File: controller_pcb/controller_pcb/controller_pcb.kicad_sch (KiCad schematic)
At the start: 31 parts, among them J1 USB_B_Micro, J2 Conn_01x04_Male, SW1 SW_MEC_5E, SW10 SW_MEC_5E, SW11 SW_MEC_5E, SW12 SW_MEC_5E, SW2 SW_MEC_5E, SW3 SW_MEC_5E, SW4 SW_MEC_5E, SW5 SW_MEC_5E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

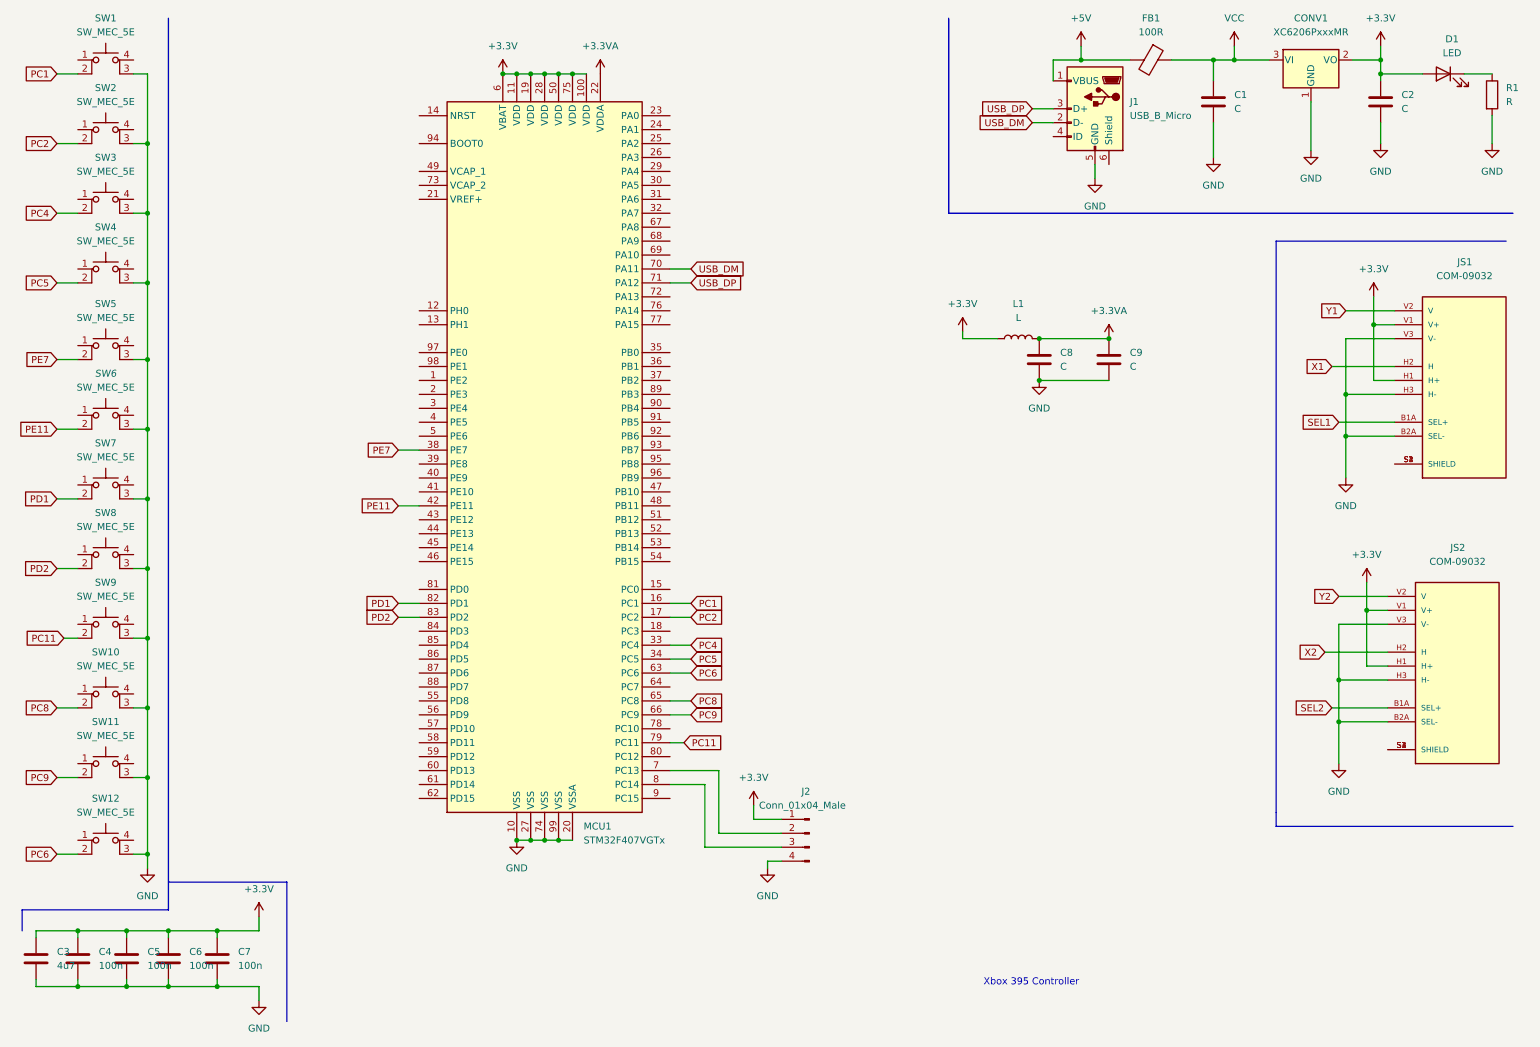
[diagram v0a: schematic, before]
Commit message: have to draw pcb
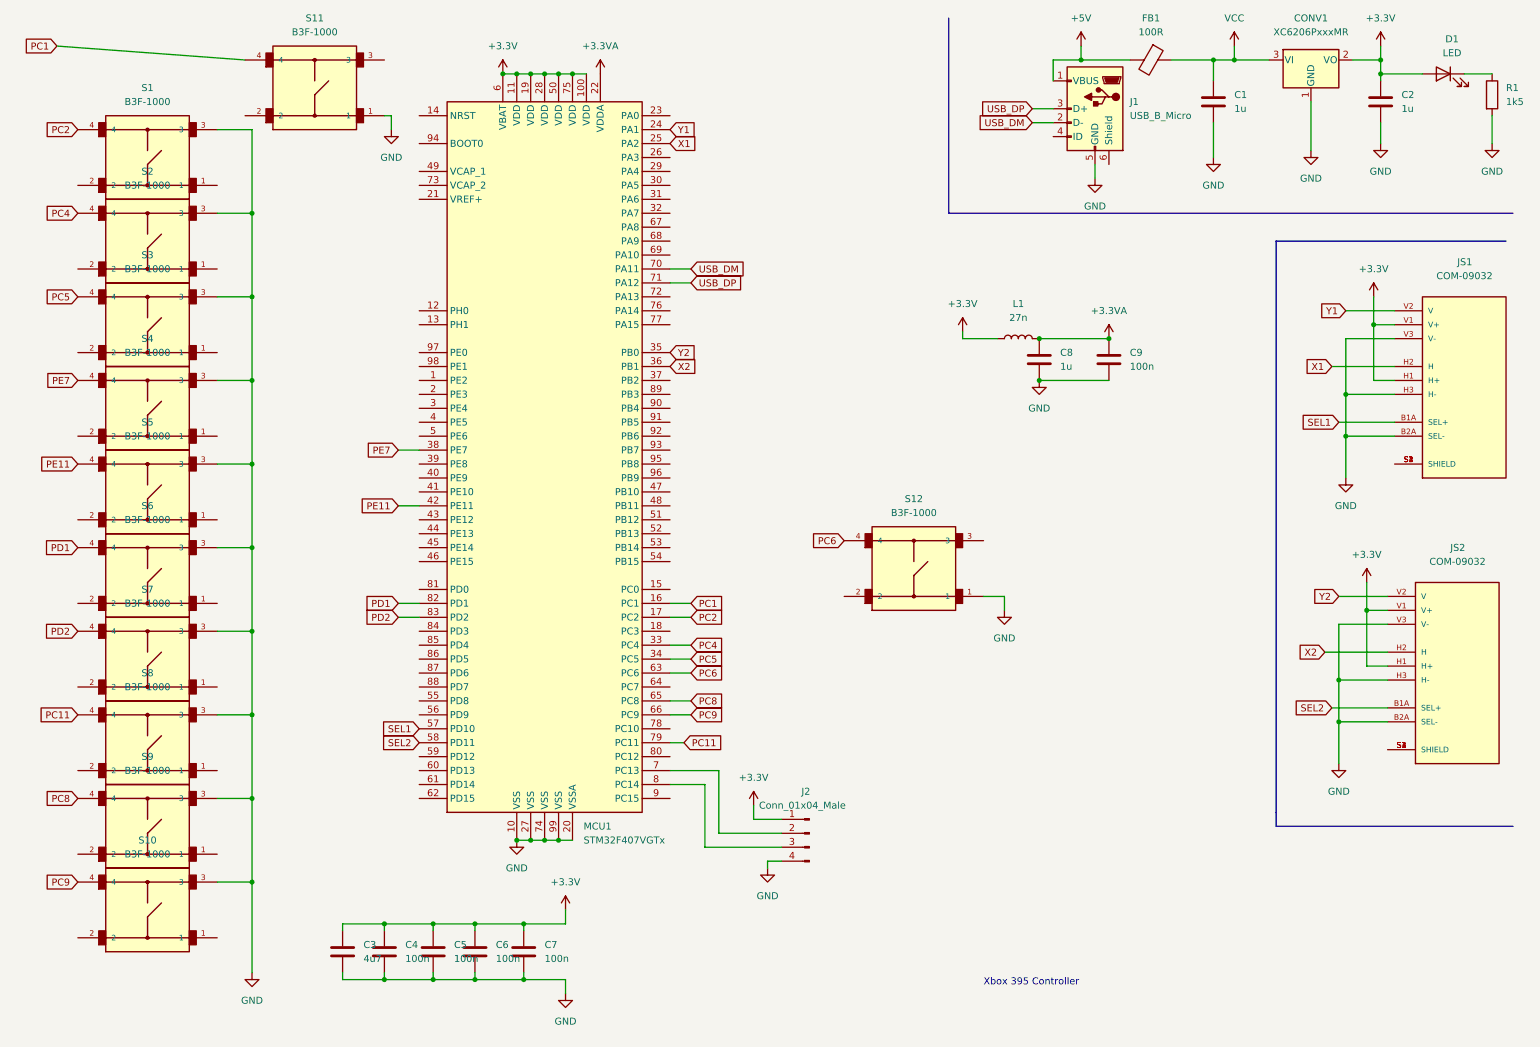
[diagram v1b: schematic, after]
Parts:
- removed SW1, SW10, SW11, SW12, SW2, SW3, SW4, SW5, SW6, SW7, SW8, SW9: SW_MEC_5E, Button_Switch_THT:SW_Tactile_Straight_KSA0Axx1LFTR, symbol Switch:SW_MEC_5E
- added S1, S10, S11, S12, S2, S3, S4, S5, S6, S7, S8, S9: B3F-1000, B3F-1000:SW_B3F-1000, symbol B3F-1000:B3F-1000
- C1, C2, C8: value C -> 1u
- C9: value C -> 100n
- L1: value L -> 27n
- R1: value R -> 1k5
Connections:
- net GND: now also S1.3, S10.3, S11.1, S12.1, S2.3, S3.3, S4.3, S5.3, S6.3, S7.3, S8.3, S9.3
- net PC1: now also S11.4
- net PC11: now also S8.4
- net PC2: now also S1.4
- net PC4: now also S2.4
- net PC5: now also S3.4
- net PC6: now also S12.4
- net PC8: now also S9.4
- net PC9: now also S10.4
- net PD1: now also S6.4
- net PD2: now also S7.4
- net PE11: now also S5.4
- net PE7: now also S4.4
- net SEL1: now also MCU1.57 (PD10)
- net SEL2: now also MCU1.58 (PD11)
- net X1: now also MCU1.25 (PA2)
- net X2: now also MCU1.36 (PB1)
- net Y1: now also MCU1.24 (PA1)
- net Y2: now also MCU1.35 (PB0)
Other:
- moved on the sheet: C3, C4, C5, C6, C7

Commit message: Updated PCB
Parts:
- removed J2: Conn_01x04_Male, Connector_PinHeader_2.54mm:PinHeader_1x04_P2.54mm_Vertical, symbol Connector:Conn_01x04_Male
- added FLASH: JTAG/SWD, symbol Connector_Generic:Conn_02x10_Odd_Even
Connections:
- net +3V3: now also FLASH.1 (Pin_1)
- net GND: now also MCU1.94 (BOOT0), FLASH.10 (Pin_10), FLASH.12 (Pin_12), FLASH.14 (Pin_14), FLASH.16 (Pin_16), FLASH.18 (Pin_18), FLASH.20 (Pin_20), FLASH.4 (Pin_4), FLASH.6 (Pin_6), FLASH.8 (Pin_8)
- net SW_DIO: now reaches MCU1.72 (PA13)
- net SW_DIO: now also FLASH.7 (Pin_7)
- net SW_CLK: now reaches MCU1.76 (PA14)
- net SW_CLK: now also FLASH.9 (Pin_9)
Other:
- moved on the sheet: S12

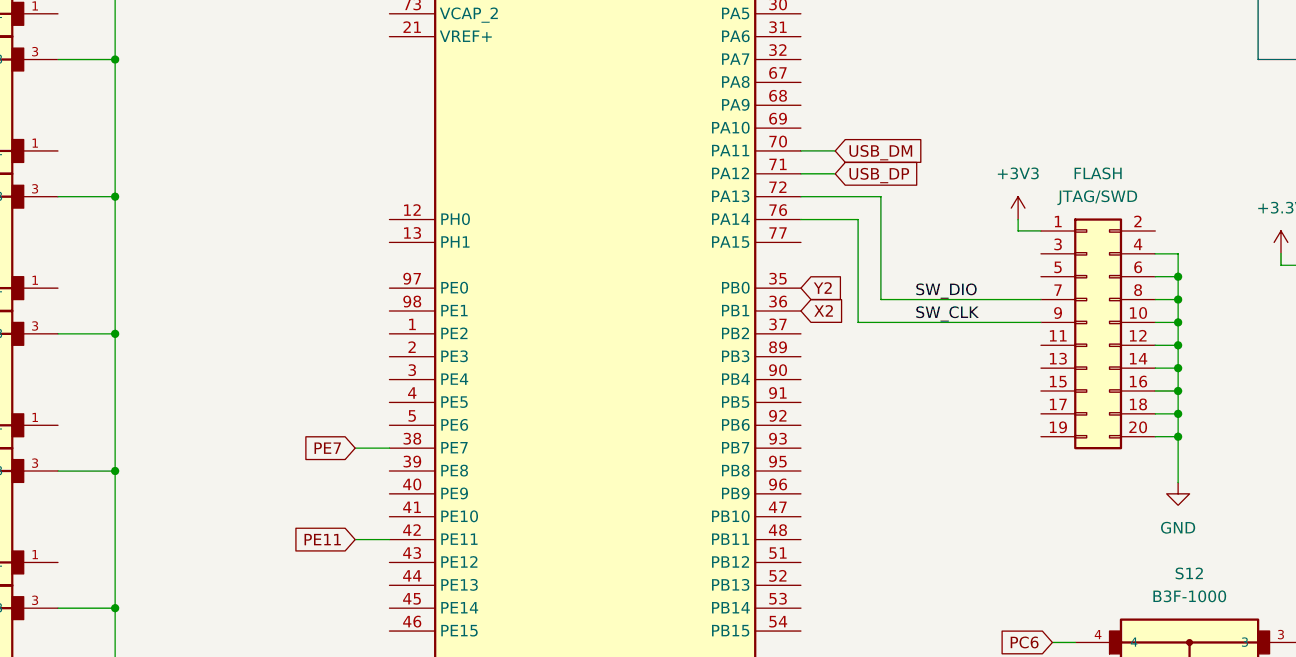
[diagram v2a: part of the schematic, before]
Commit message: started wiring schematic
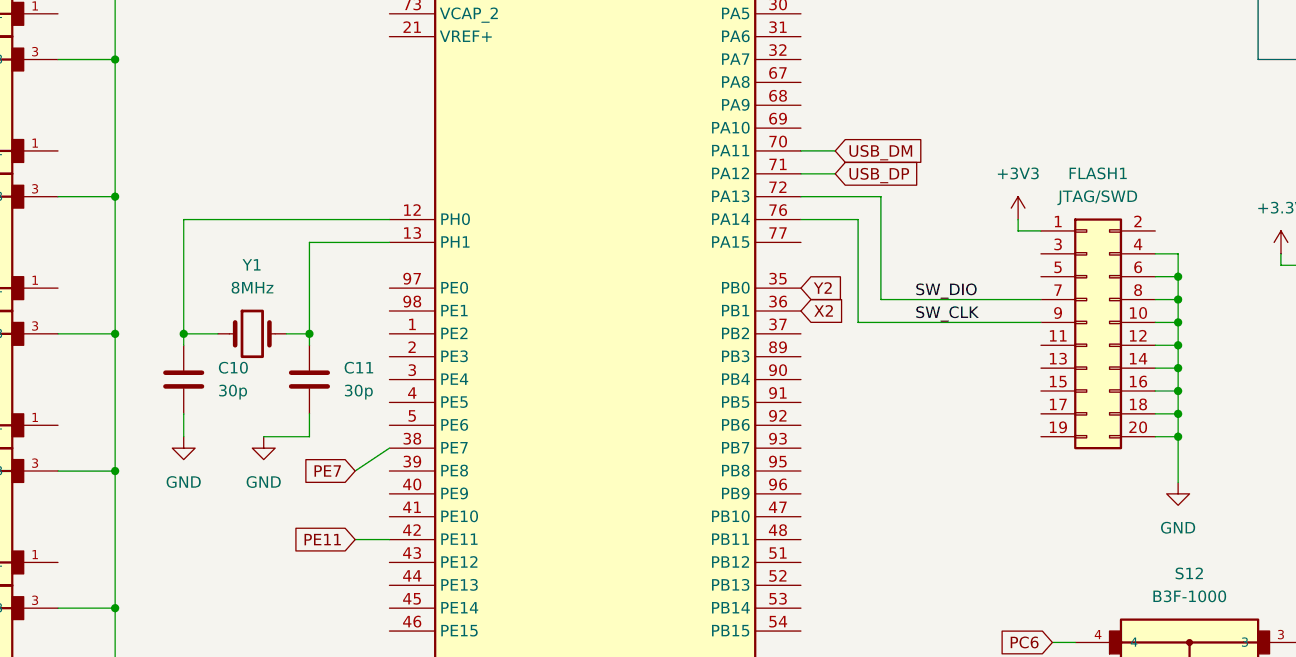
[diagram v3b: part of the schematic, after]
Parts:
- added C10, C11: 30p, Capacitor_SMD:C_0805_2012Metric, symbol Device:C
- added Y1: 8MHz, Crystal:Crystal_SMD_5032-2Pin_5.0x3.2mm, symbol Device:Crystal
- FB1: footprint Inductor_SMD:L_0603_1608Metric -> Resistor_SMD:R_0805_2012Metric
- FLASH1: renamed from FLASH; footprint (none) -> Connector_PinHeader_2.54mm:PinHeader_2x10_P2.54mm_Vertical
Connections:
- net GND: now also C10.2, C11.2
- net at MCU1.12 (PH0): now also C10.1, Y1.1
- net at MCU1.13 (PH1): now also C11.1, Y1.2

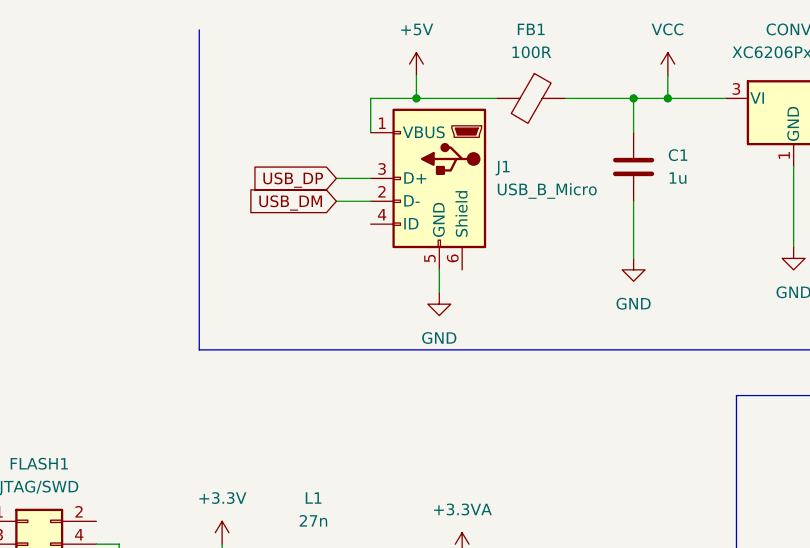
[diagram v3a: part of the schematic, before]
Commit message: fixed drc warnings and errors in pcb
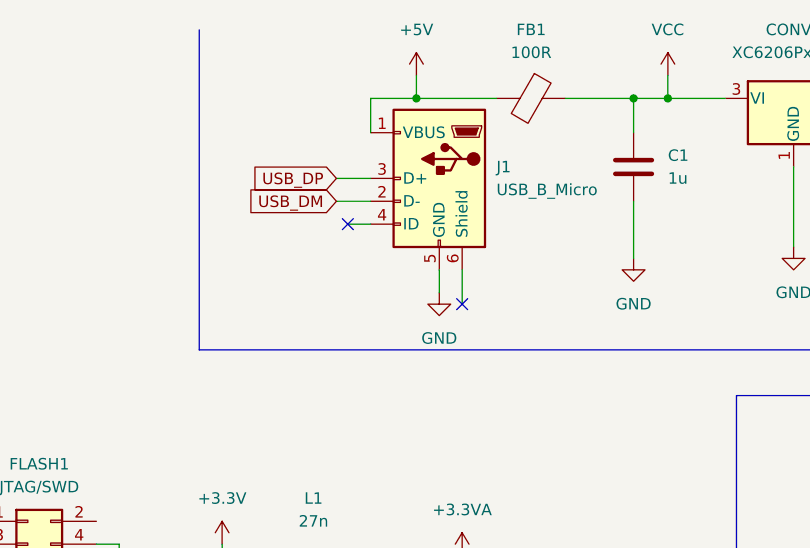
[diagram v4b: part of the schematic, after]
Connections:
- no-connect marks 0 -> 2
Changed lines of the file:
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@@
   (junction (at 54.61 140.97) (diameter 0) (color 0 0 0 0)
   )
+  (no_connect (at 210.82 44.45))
+  (no_connect (at 198.12 35.56))
   (wire (pts (xy 54.61 95.25) (xy 54.61 110.49))
     (stroke (width 0) (type default) (color 0 0 0 0))
@@
     (stroke (width 0) (type default) (color 0 0 0 0))
   )
+  (wire (pts (xy 198.12 35.56) (xy 200.66 35.56))
+    (stroke (width 0) (type default) (color 0 0 0 0))
+  )
   (wire (pts (xy 82.55 36.83) (xy 82.55 31.75))
     (stroke (width 0) (type default) (color 0 0 0 0))
@@
     (stroke (width 0) (type default) (color 0 0 0 0))
   )
+  (wire (pts (xy 210.82 40.64) (xy 210.82 44.45))
+    (stroke (width 0) (type default) (color 0 0 0 0))
+  )
